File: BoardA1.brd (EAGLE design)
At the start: 44 x 93 mm, 23 parts, among them J1 LOAD_CELL1X03-PTH, J2 FEMALE 2x3, J3 LOAD_CELL1X03-PTH, J5 LOAD_CELL1X03-PTH, J6 LOAD_CELL1X03-PTH

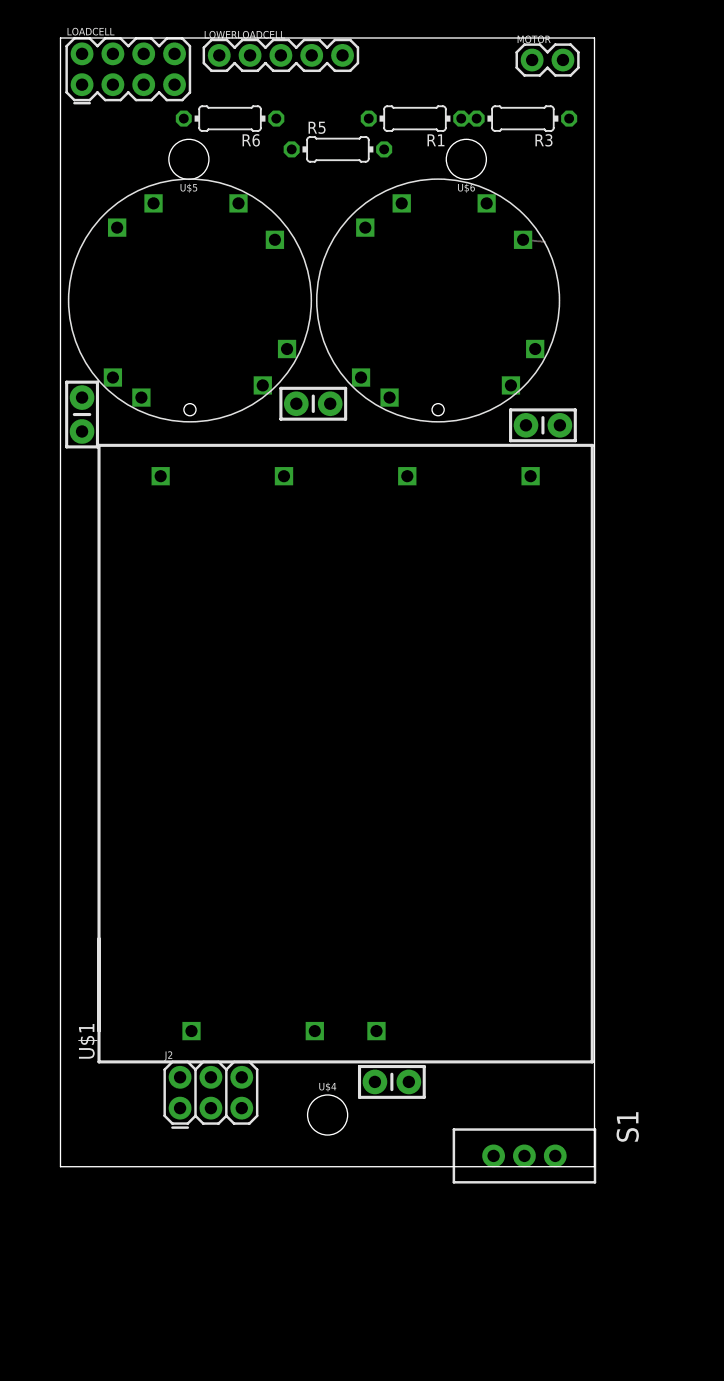
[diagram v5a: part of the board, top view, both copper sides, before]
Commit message: moved motor connector
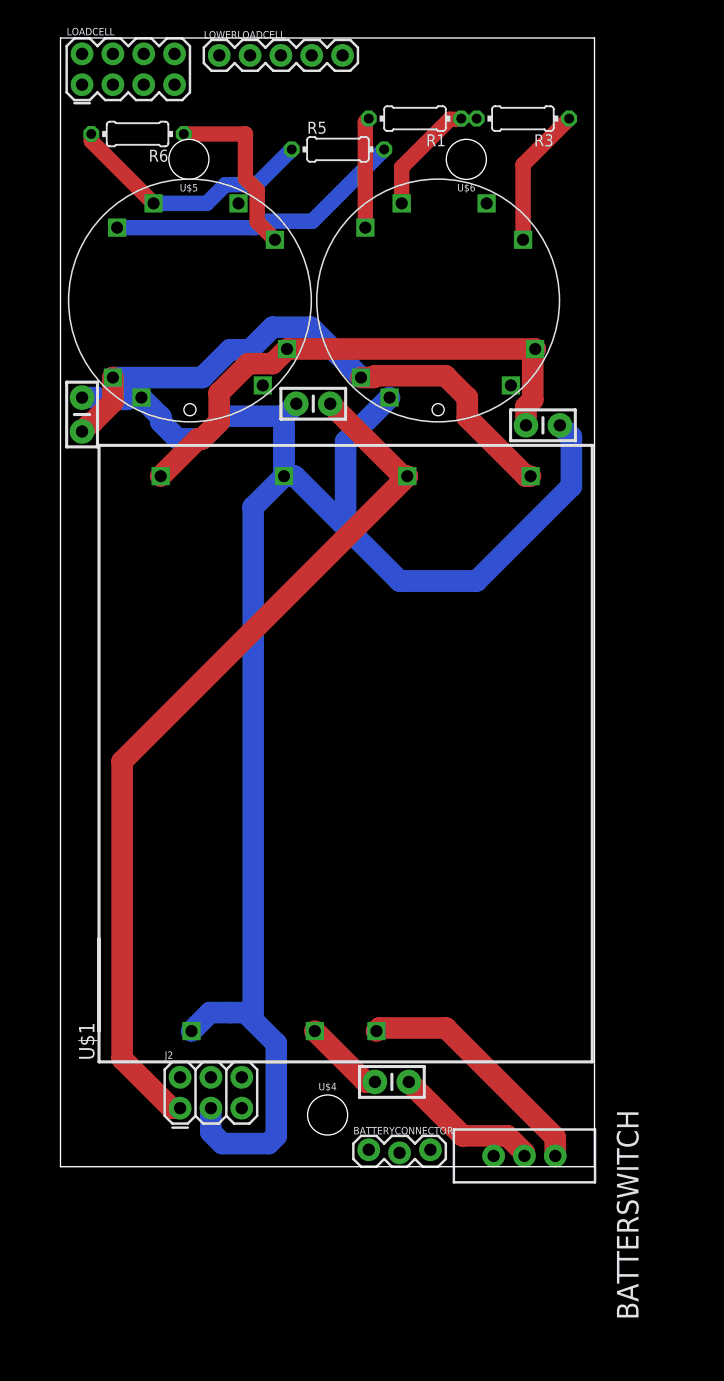
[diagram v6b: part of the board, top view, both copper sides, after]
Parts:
- removed MOTOR: (no value), SparkFun-Connectors:1X02
- added BATTERYCONNECTOR: (no value), SparkFun-Connectors:1X03_LOCK
- moved R6 7.73 mm to (6.35, 85.1)
- renumbered S1 to BATTERSWITCH
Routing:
- net GND: track 0.00 -> 143.7 mm
- net 5V: track 0.00 -> 73.0 mm
- net +15V: track 0.00 -> 47.7 mm
- net -15V: track 0.00 -> 43.2 mm
- net +EX2: track 0.00 -> 24.7 mm
- net +SIG2: track 0.00 -> 21.1 mm
- net N$3: track 0.00 -> 20.1 mm
- net -EX2: track 0.00 -> 14.8 mm
- net N$1: track 0.00 -> 12.2 mm
- net -EX1: track 1.82 -> 11.6 mm
- net +SIG1: track 0.00 -> 9.54 mm
- net +EX1: track 0.00 -> 9.10 mm
- net N$2: track 0.00 -> 6.69 mm

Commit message: Teensy Pin Update2
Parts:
- removed LOWERLOADCELL: (no value), SparkFun-Connectors:1X05
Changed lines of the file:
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@@
 <grid distance="50" unitdist="mil" unit="mil" style="dots" multiple="1" display="yes" altdistance="5" altunitdist="mil" altunit="mil"/>
 <layers>
-<layer number="1" name="Top" color="4" fill="1" visible="yes" active="yes"/>
+<layer number="1" name="Top" color="4" fill="1" visible="no" active="yes"/>
 <layer number="2" name="Route2" color="1" fill="3" visible="no" active="no"/>
 <layer number="3" name="Route3" color="4" fill="3" visible="no" active="no"/>
@@
 <layer number="14" name="Route14" color="1" fill="6" visible="no" active="no"/>
 <layer number="15" name="Route15" color="4" fill="6" visible="no" active="no"/>
-<layer number="16" name="Bottom" color="1" fill="1" visible="yes" active="yes"/>
+<layer number="16" name="Bottom" color="1" fill="1" visible="no" active="yes"/>
 <layer number="17" name="Pads" color="2" fill="1" visible="yes" active="yes"/>
 <layer number="18" name="Vias" color="2" fill="1" visible="yes" active="yes"/>
@@
 <element name="U$5" library="SparkFun-Hardware" package="STAND-OFF" value="" x="10.58" y="83" rot="R180"/>
 <element name="U$6" library="SparkFun-Hardware" package="STAND-OFF" value="" x="33.44" y="83" rot="R180"/>
-<element name="LOWERLOADCELL" library="SparkFun-Connectors" package="1X05" value="" x="13.081" y="91.567"/>
 <element name="LOADCELL" library="SparkFun-Connectors" package="2X4" value="" x="5.588" y="90.424"/>
 <element name="BATTERYCONNECTOR" library="SparkFun-Connectors" package="1X03_LOCK" value="" x="25.4" y="1.27"/>

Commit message: dxf files
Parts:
- moved R6 10.5 mm to (16.5, 87.6)
- moved C2 5.34 mm to (1.52, 56.6)
- moved R3 4.20 mm to (37.8, 90.6)
- moved R1 2.84 mm to (27.9, 88.9)
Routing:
- net +15V: track 47.7 -> 62.7 mm
- net +SIG2: track 21.1 -> 31.1 mm
- net GND: track 143.7 -> 148.6 mm
- net -EX1: track 11.6 -> 14.9 mm
- net +EX1: track 9.10 -> 12.3 mm
- net +SIG1: track 9.54 -> 12.3 mm
- net -EX2: track 14.8 -> 15.4 mm
